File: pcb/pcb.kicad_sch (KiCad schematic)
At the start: 23 parts, among them J1 USB_C_Receptacle_USB2.0_16P, SW1 SW_Push, U1 USBLC6-2SC6, U2 ATmega32U4-A, U3 STM32F072C8Tx, Y1 16MHz

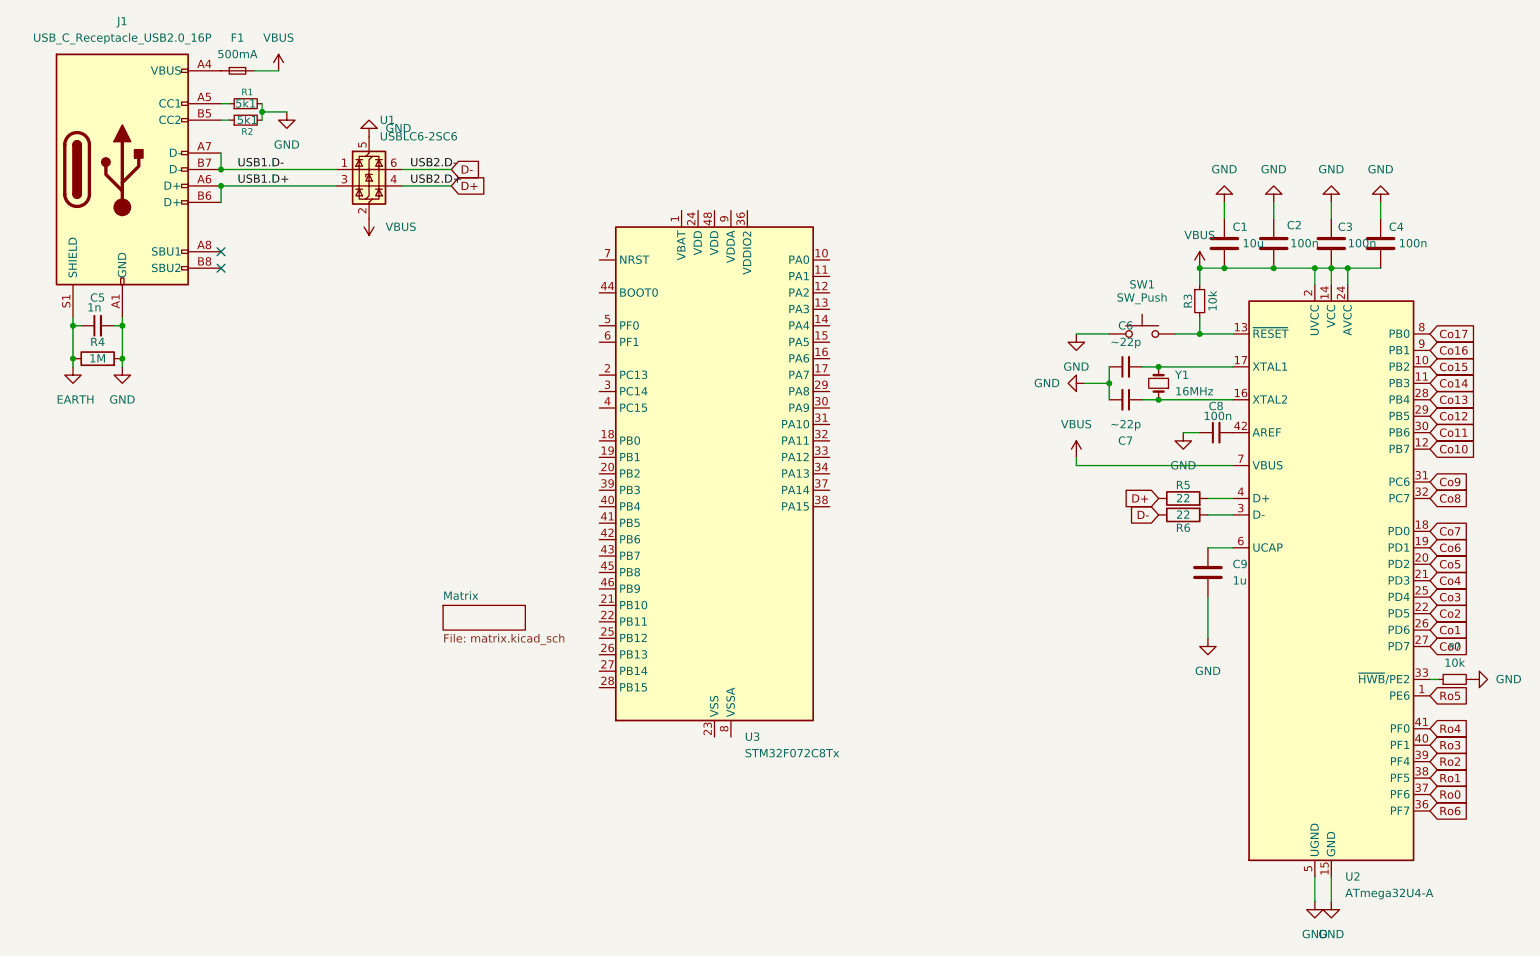
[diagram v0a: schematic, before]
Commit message: change MCU to STM32F0
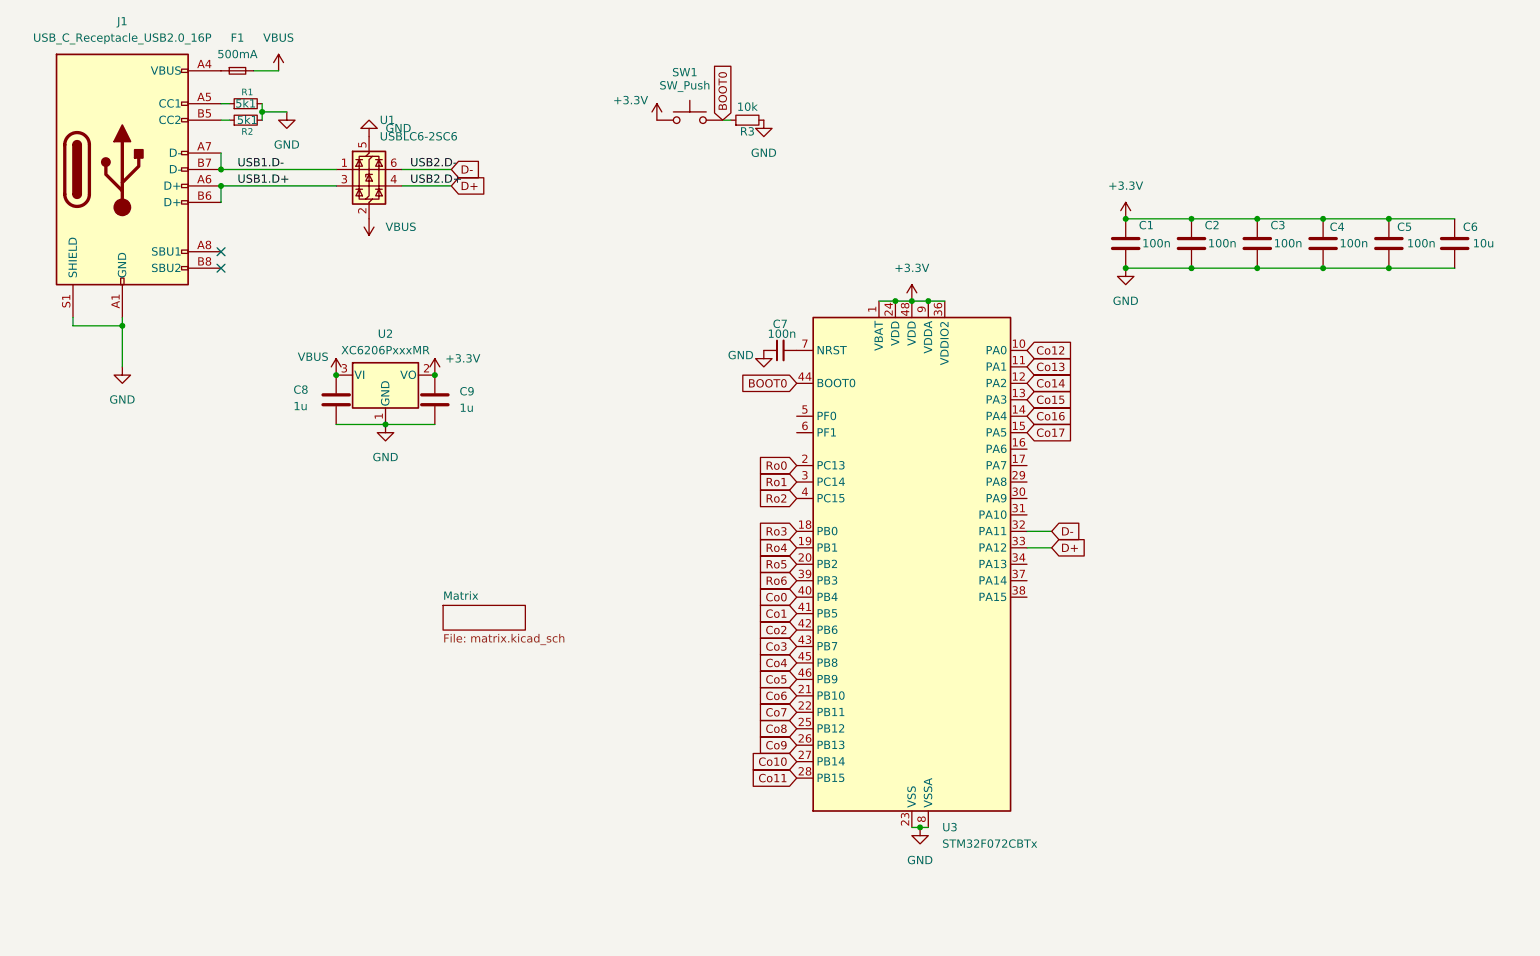
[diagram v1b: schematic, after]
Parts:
- removed C5: 1n, Capacitor_SMD:C_01005_0402Metric, symbol Device:C_Small
- removed C6, C7: ~22p, Capacitor_SMD:C_0402_1005Metric, symbol Device:C_Small
- removed R4: 1M, Resistor_SMD:R_0201_0603Metric, symbol Device:R
- removed R5, R6: 22, Resistor_SMD:R_0402_1005Metric, symbol Device:R
- removed R7: 10k, Resistor_SMD:R_01005_0402Metric, symbol Device:R_Small
- removed U2: ATmega32U4-A, Package_QFP:TQFP-44_10x10mm_P0.8mm, symbol MCU_Microchip_ATmega:ATmega32U4-A
- removed U3: STM32F072C8Tx, Package_QFP:LQFP-48_7x7mm_P0.5mm, symbol MCU_ST_STM32F0:STM32F072C8Tx
- removed Y1: 16MHz, Crystal:Crystal_SMD_0603-2Pin_6.0x3.5mm, symbol Device:Crystal_Small
- added C1, C2: 100n, Capacitor_SMD:C_0402_1005Metric, symbol Device:C
- added C8: 1u, Capacitor_SMD:C_0603_1608Metric, symbol Device:C
- added U2: XC6206PxxxMR, Package_TO_SOT_SMD:SOT-23-3, symbol Regulator_Linear:XC6206PxxxMR
- added U3: STM32F072CBTx, Package_QFP:LQFP-48_7x7mm_P0.5mm, symbol MCU_ST_STM32F0:STM32F072CBTx
- C9: footprint Capacitor_SMD:C_0402_1005Metric -> Capacitor_SMD:C_0603_1608Metric
- renumbered C2 to C3, C3 to C4, C4 to C5, C1 to C6, C8 to C7
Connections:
- net EARTH is gone; now on net GND: J1.S1 (SHIELD)
- net Co0: now also U3.40 (PB4)
- net Co1: now also U3.41 (PB5)
- net Co10: now also U3.27 (PB14)
- net Co11: now also U3.28 (PB15)
- net Co12: now also U3.10 (PA0)
- net Co13: now also U3.11 (PA1)
- net Co14: now also U3.12 (PA2)
- net Co15: now also U3.13 (PA3)
- net Co16: now also U3.14 (PA4)
- net Co17: now also U3.15 (PA5)
- net Co2: now also U3.42 (PB6)
- net Co3: now also U3.43 (PB7)
- net Co4: now also U3.45 (PB8)
- net Co5: now also U3.46 (PB9)
- net Co6: now also U3.21 (PB10)
- net Co7: now also U3.22 (PB11)
- net Co8: now also U3.25 (PB12)
- net Co9: now also U3.26 (PB13)
- net D+: now also U3.33 (PA12)
- net D-: now also U3.32 (PA11)
- net GND: now also C3.2, C4.2, C5.2, C6.2, R3.2, C1.2, C2.2, C8.2, U2.1 (GND), U3.23 (VSS), U3.35 (VSS), U3.47 (VSS), U3.8 (VSSA); no longer C3.1, C4.1, C5.1, C6.1, SW1.1
- net Ro0: now also U3.2 (PC13)
- net Ro1: now also U3.3 (PC14)
- net Ro2: now also U3.4 (PC15)
- net Ro3: now also U3.18 (PB0)
- net Ro4: now also U3.19 (PB1)
- net Ro5: now also U3.20 (PB2)
- net Ro6: now also U3.39 (PB3)
- net VBUS: now also C8.1, U2.3 (VI); no longer C3.2, C4.2, C5.2, C6.2, R3.1
- net +3.3V: now reaches C9.1
- net +3.3V: now also C3.1, C4.1, C5.1, C6.1, SW1.1, C1.1, C2.1, U2.2 (VO), U3.1 (VBAT), U3.24 (VDD), U3.36 (VDDIO2), U3.48 (VDD), U3.9 (VDDA)
- net BOOT0: now reaches SW1.2
- net BOOT0: now also R3.1, U3.44 (BOOT0); no longer R3.2
- net at C7.2: now also U3.7 (NRST)
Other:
- moved on the sheet: C3, C4, C5, C6, C7, R3, SW1

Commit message: ESD protection
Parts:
- U1: footprint PCM_marbastlib-various:SOT-23-6-routable -> Package_TO_SOT_SMD:SOT-23-6
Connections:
- net GND: now also U1.2 (GND); no longer U1.5 (VBUS)
- net VBUS: now also U1.5 (VBUS); no longer U1.2 (GND)
- net USB1.D+ renamed usb+
- net USB1.D- renamed usb-

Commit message: Connecting MCU
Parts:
- removed C8, C9: 1u, Capacitor_SMD:C_0603_1608Metric, symbol Device:C
- added C8, C9: 1u, Capacitor_SMD:C_0402_1005Metric, symbol Device:C_Small
- F1: value 500mA -> 500m
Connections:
- net +3.3V: now also C9.1
- net D+: now also J1.A6 (D+), J1.B6 (D+), U1.1 (I/O1), U1.6 (I/O1); no longer U1.4 (I/O2)
- net D-: now also J1.A7 (D-), J1.B7 (D-), U1.3 (I/O2), U1.4 (I/O2); no longer U1.6 (I/O1)
- net GND: now also C8.2, C9.2
- net VBUS: now also C8.1
- removed net usb+: J1.A6 (D+), J1.B6 (D+), U1.3 (I/O2)
- removed net usb-: J1.A7 (D-), J1.B7 (D-), U1.1 (I/O1)

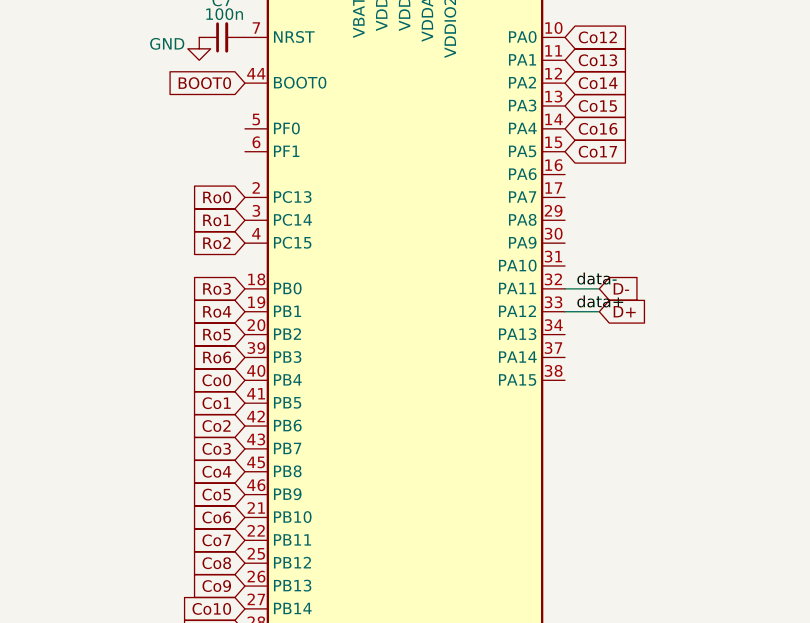
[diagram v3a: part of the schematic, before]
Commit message: Connects all components on the PCB
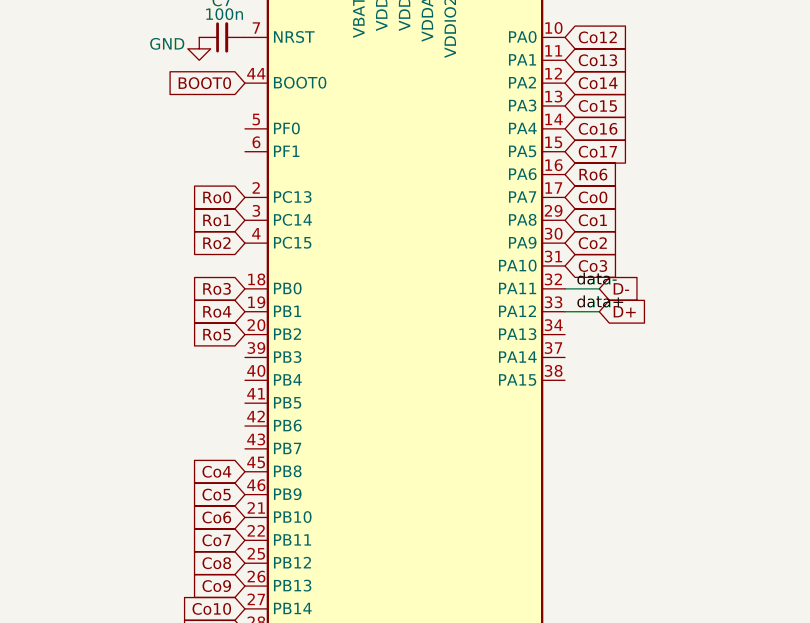
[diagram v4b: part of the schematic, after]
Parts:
- C7: footprint Capacitor_SMD:C_01005_0402Metric -> Capacitor_SMD:C_0201_0603Metric
- SW1: footprint Button_Switch_SMD:SW_SPST_TL3342 -> PCM_marbastlib-various:SW_SPST_SKQG_WithStem
- U1: footprint Package_TO_SOT_SMD:SOT-23-6 -> PCM_marbastlib-various:SOT-23-6-routable
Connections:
- net Co0: now also U3.17 (PA7); no longer U3.40 (PB4)
- net Co1: now also U3.29 (PA8); no longer U3.41 (PB5)
- net Co2: now also U3.30 (PA9); no longer U3.42 (PB6)
- net Co3: now also U3.31 (PA10); no longer U3.43 (PB7)
- net Ro6: now also U3.16 (PA6); no longer U3.39 (PB3)

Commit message: Matrix ready
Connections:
- net Co17: now also U3.45 (PB8); no longer U3.15 (PA5)
- net Co4: now also U3.15 (PA5); no longer U3.45 (PB8)

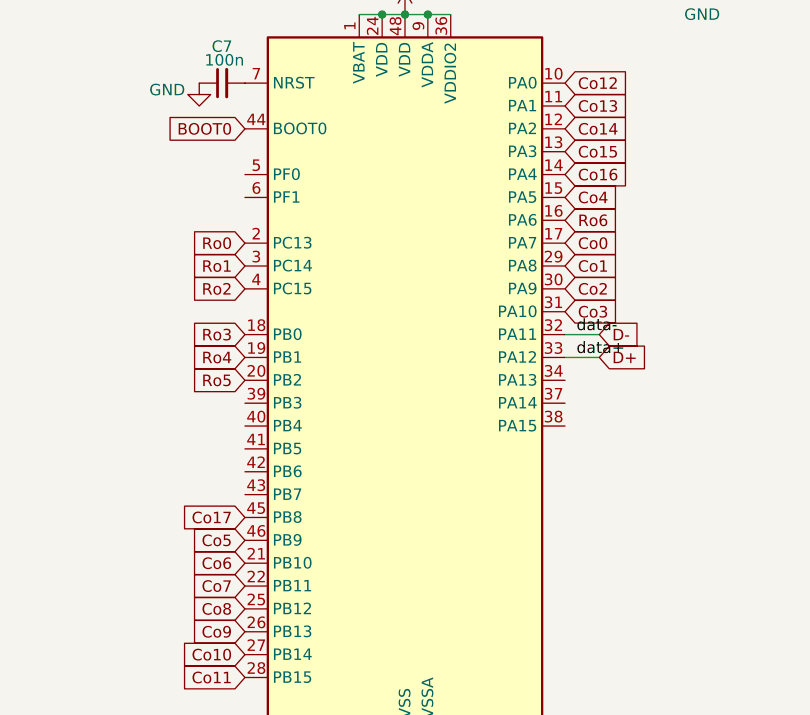
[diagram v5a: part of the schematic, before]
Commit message: Change generic diodes to SOD-123
50% done
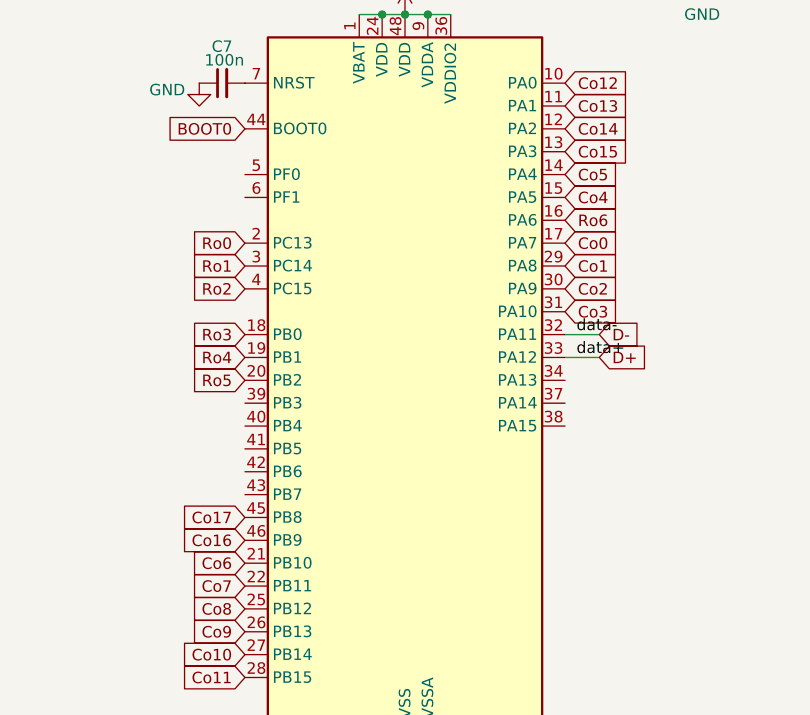
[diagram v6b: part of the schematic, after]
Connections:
- net Co16: now also U3.46 (PB9); no longer U3.14 (PA4)
- net Co5: now also U3.14 (PA4); no longer U3.46 (PB9)
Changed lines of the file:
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@@
 	(global_label "Co5"
+		(shape input)
+		(at 181.61 78.74 0)
+		(fields_autoplaced yes)
+		(effects
+			(font
+				(size 1.27 1.27)
+			)
+			(justify left)
+		)
+		(property "Intersheetrefs" "${INTERSHEET_REFS}"
+			(at 188.2237 78.74 0)
+			(effects
+				(font
+					(size 1.27 1.27)
+				)
+				(justify left)
+				(hide yes)
+			)
+		)
+	)
+	(global_label "Co16"
 		(shape input)
 		(at 146.05 119.38 180)
@@
 		)
 		(property "Intersheetrefs" "${INTERSHEET_REFS}"
-			(at 139.4363 119.38 0)
+			(at 138.2268 119.38 0)
 			(effects
 				(font
@@
 				(hide yes)
 			)
-		)
-	)
-	(global_label "Co16"
-		(shape input)
-		(at 181.61 78.74 0)
-		(fields_autoplaced yes)
-		(effects
-			(font
-				(size 1.27 1.27)
-			)
-			(justify left)
-		)
-		(property "Intersheetrefs" "${INTERSHEET_REFS}"
-			(at 189.4332 78.74 0)
-			(effects
-				(font
-					(size 1.27 1.27)
-				)
-				(justify left)
-				(hide yes)
-			)

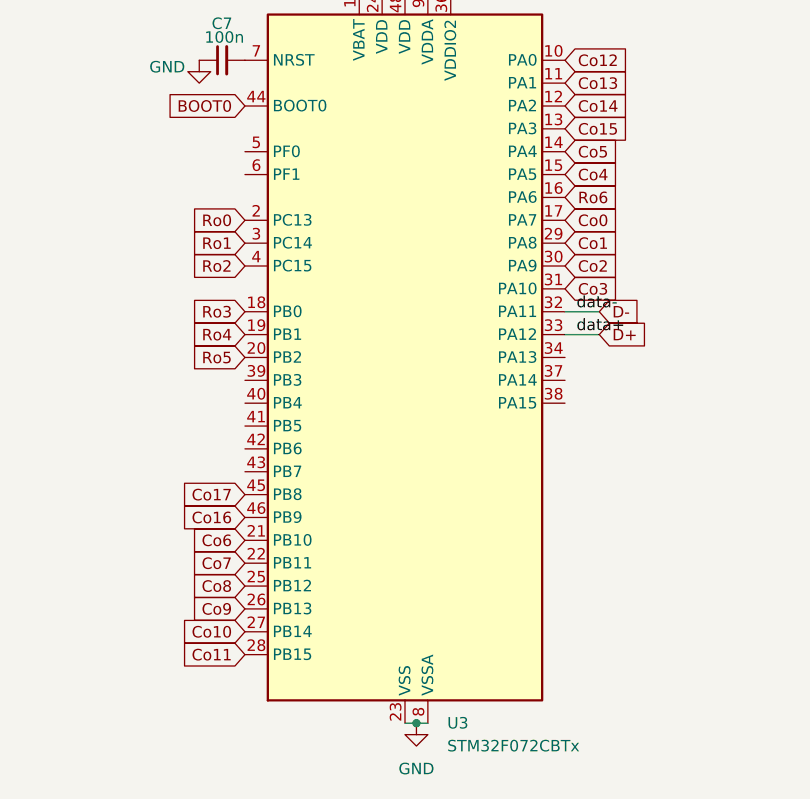
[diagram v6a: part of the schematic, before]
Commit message: finished diodes and finished top MCU datalines
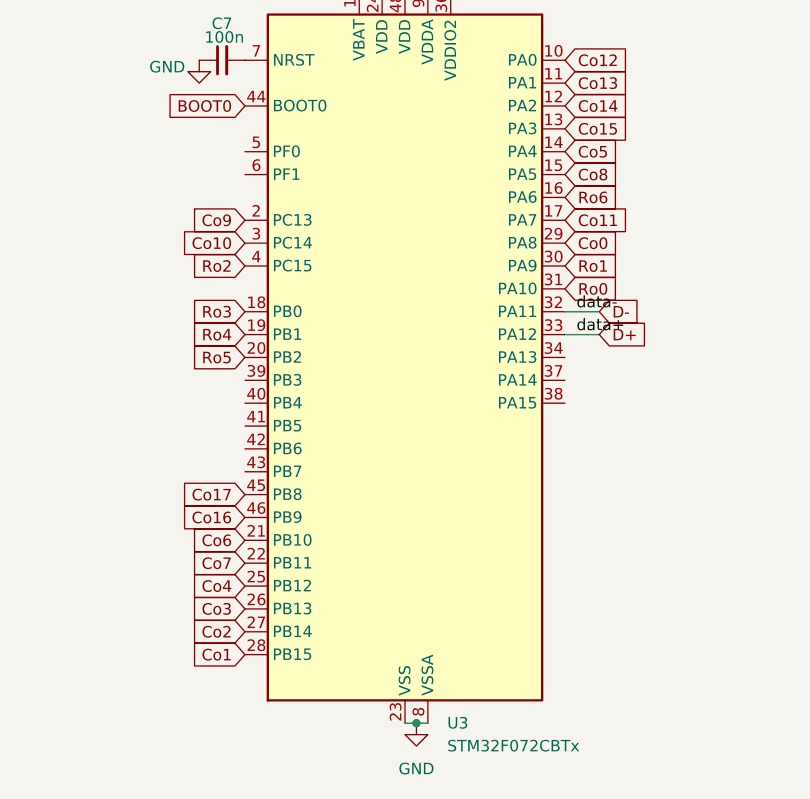
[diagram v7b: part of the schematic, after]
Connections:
- net Co0: now also U3.29 (PA8); no longer U3.17 (PA7)
- net Co1: now also U3.28 (PB15); no longer U3.29 (PA8)
- net Co10: now also U3.3 (PC14); no longer U3.27 (PB14)
- net Co11: now also U3.17 (PA7); no longer U3.28 (PB15)
- net Co2: now also U3.27 (PB14); no longer U3.30 (PA9)
- net Co3: now also U3.26 (PB13); no longer U3.31 (PA10)
- net Co4: now also U3.25 (PB12); no longer U3.15 (PA5)
- net Co8: now also U3.15 (PA5); no longer U3.25 (PB12)
- net Co9: now also U3.2 (PC13); no longer U3.26 (PB13)
- net Ro0: now also U3.31 (PA10); no longer U3.2 (PC13)
- net Ro1: now also U3.30 (PA9); no longer U3.3 (PC14)
